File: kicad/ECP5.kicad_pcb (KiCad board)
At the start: 4 copper layers, 64.4 x 54.6 mm, 28 parts, among them J1 FLE-126-01-G-DV, SW1 PTS645SK43SMTR92 LFS

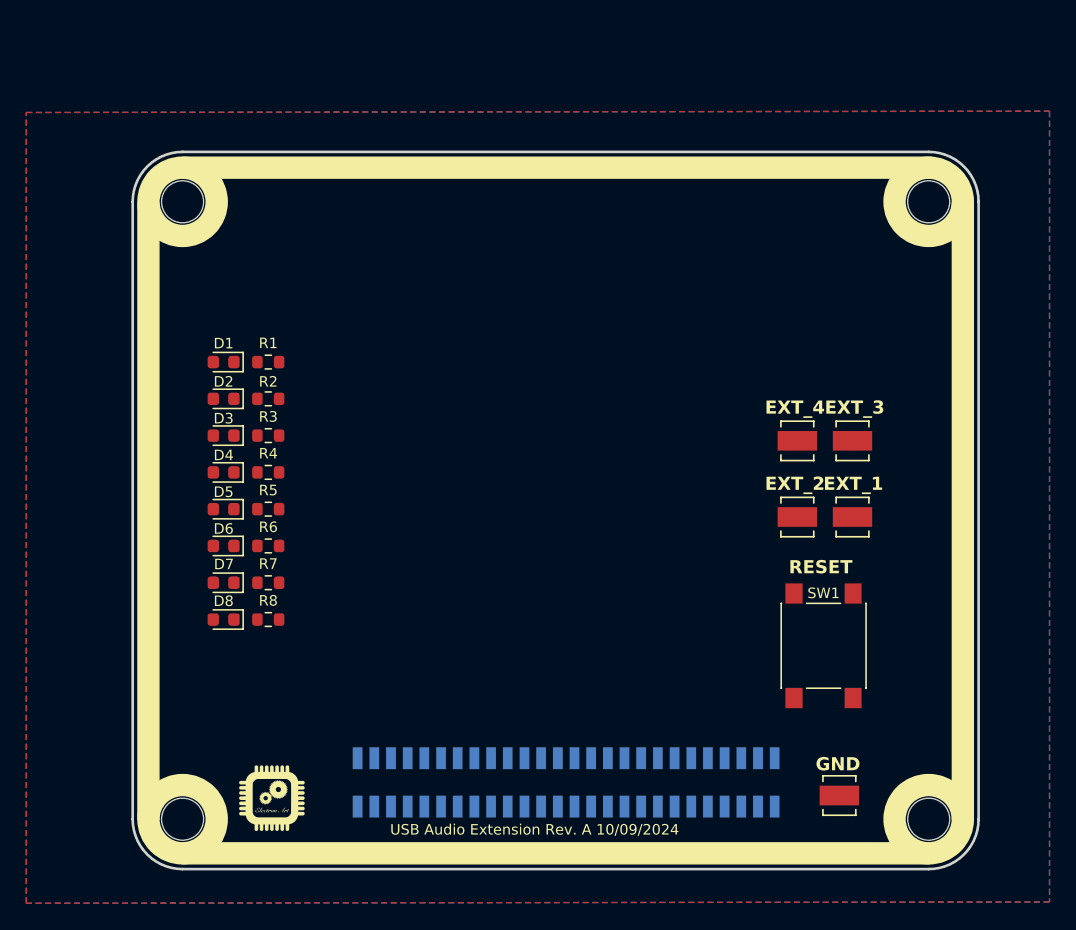
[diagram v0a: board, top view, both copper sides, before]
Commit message: First pass at arranging components
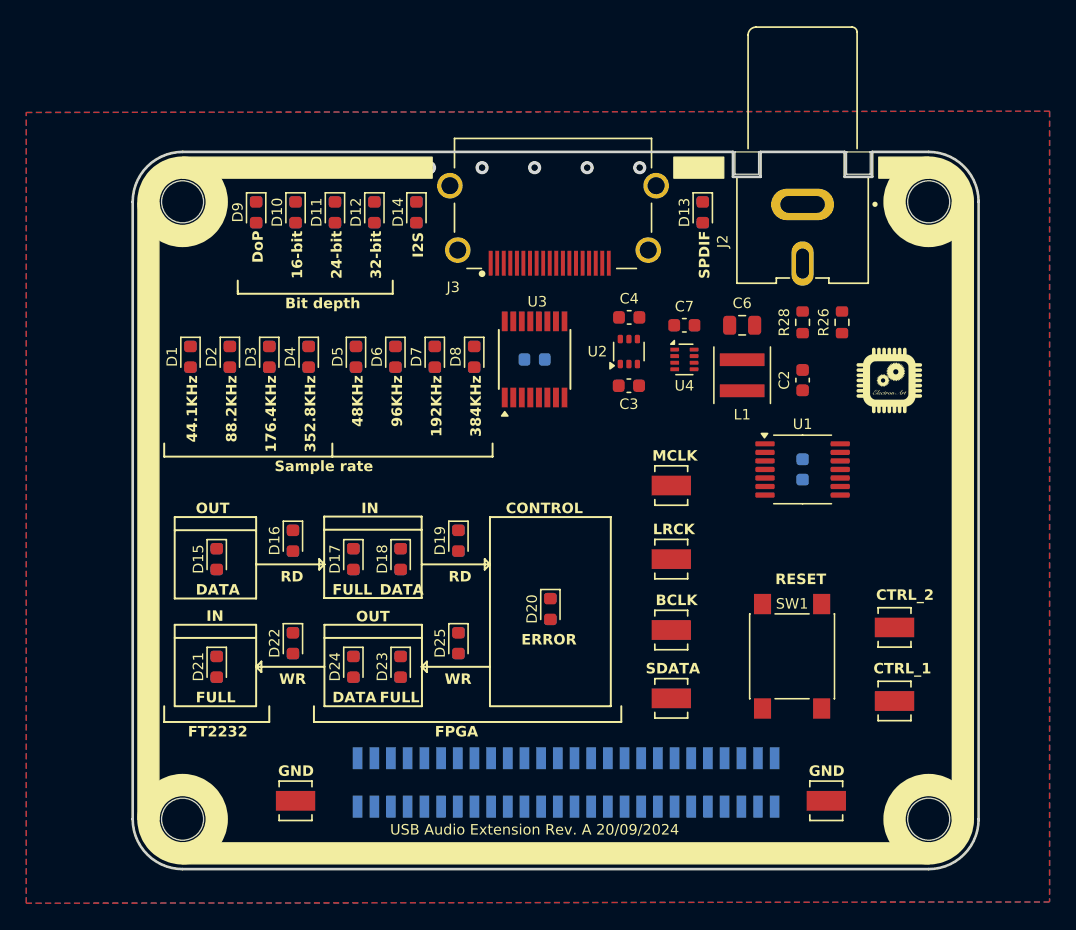
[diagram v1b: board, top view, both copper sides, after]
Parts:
- added C1: 0.1µF, Capacitor_SMD:C_0603_1608Metric, B.Cu at (168.0, 93.6)
- added C2: 0.1µF, Capacitor_SMD:C_0603_1608Metric, F.Cu at (168.0, 86.8)
- added C3: 4.7µF, Capacitor_SMD:C_0603_1608Metric, F.Cu at (154.8, 87.2)
- added C4: 18nF, Capacitor_SMD:C_0603_1608Metric, F.Cu at (154.8, 82.0)
- added C5: 0.1µF, Capacitor_SMD:C_0603_1608Metric, B.Cu at (147.6, 85.2)
- added C6: 10µF, Capacitor_SMD:C_0805_2012Metric, F.Cu at (163.4, 82.6)
- added C7: 4.7µF, Capacitor_SMD:C_0603_1608Metric, F.Cu at (159.0, 82.6)
- added D10: BLUE, LED_SMD:LED_0603_1608Metric, F.Cu at (129.4, 74.0)
- added D11: BLUE, LED_SMD:LED_0603_1608Metric, F.Cu at (132.4, 74.0)
- added D12: BLUE, LED_SMD:LED_0603_1608Metric, F.Cu at (135.4, 74.0)
- added D13: GREEN, LED_SMD:LED_0603_1608Metric, F.Cu at (160.4, 74.0)
- added D14: GREEN, LED_SMD:LED_0603_1608Metric, F.Cu at (138.6, 74.0)
- added D15: GREEN, LED_SMD:LED_0603_1608Metric, F.Cu at (123.4, 100.4)
- added D16: GREEN, LED_SMD:LED_0603_1608Metric, F.Cu at (129.2, 99.0)
- added D17: YELLOW, LED_SMD:LED_0603_1608Metric, F.Cu at (133.8, 100.4)
- added D18: GREEN, LED_SMD:LED_0603_1608Metric, F.Cu at (137.4, 100.4)
- added D19: BLUE, LED_SMD:LED_0603_1608Metric, F.Cu at (141.8, 99.0)
- added D20: RED, LED_SMD:LED_0603_1608Metric, F.Cu at (148.8, 104.2)
- added D21: YELLOW, LED_SMD:LED_0603_1608Metric, F.Cu at (123.4, 108.6)
- added D22: GREEN, LED_SMD:LED_0603_1608Metric, F.Cu at (129.2, 106.8)
- added D23: YELLOW, LED_SMD:LED_0603_1608Metric, F.Cu at (137.4, 108.6)
- added D24: GREEN, LED_SMD:LED_0603_1608Metric, F.Cu at (133.8, 108.6)
- added D25: BLUE, LED_SMD:LED_0603_1608Metric, F.Cu at (141.8, 106.8)
- added D9: BLUE, LED_SMD:LED_0603_1608Metric, F.Cu at (126.4, 74.0)
- added J2: RCJ-044, ECP5_BGA381_FT2232HQ_FIFO_EXT:CUI_RCJ-042, F.Cu at (168.0, 69.4)
- added J3: HDMI_A, ECP5_BGA381_FT2232HQ_FIFO_EXT:AMPHENOL_10029449-001RLF, F.Cu at (149.0, 76.9)
- added L1: 1µH, Inductor_SMD:L_Coilcraft_XxL4040, F.Cu at (163.4, 86.4)
- added R10: 330, Resistor_SMD:R_0603_1608Metric, B.Cu at (129.4, 74.0)
- added R11: 330, Resistor_SMD:R_0603_1608Metric, B.Cu at (132.4, 74.0)
- added R12: 330, Resistor_SMD:R_0603_1608Metric, B.Cu at (135.4, 74.0)
- added R13: 330, Resistor_SMD:R_0603_1608Metric, B.Cu at (160.4, 74.0)
- added R14: 330, Resistor_SMD:R_0603_1608Metric, B.Cu at (138.6, 74.0)
- added R15: 330, Resistor_SMD:R_0603_1608Metric, B.Cu at (123.4, 100.4)
- added R16: 330, Resistor_SMD:R_0603_1608Metric, B.Cu at (129.2, 99.0)
- added R17: 750, Resistor_SMD:R_0603_1608Metric, B.Cu at (133.8, 100.4)
- added R18: 330, Resistor_SMD:R_0603_1608Metric, B.Cu at (137.4, 100.4)
- added R20: 750, Resistor_SMD:R_0603_1608Metric, B.Cu at (148.8, 104.2)
- added R21: 750, Resistor_SMD:R_0603_1608Metric, B.Cu at (123.4, 108.6)
- added R22: 330, Resistor_SMD:R_0603_1608Metric, B.Cu at (129.2, 106.8)
- added R23: 750, Resistor_SMD:R_0603_1608Metric, B.Cu at (137.4, 108.6)
- added R24: 330, Resistor_SMD:R_0603_1608Metric, B.Cu at (133.8, 108.6)
- added R26: 150, Resistor_SMD:R_0603_1608Metric, F.Cu at (171.0, 82.4)
- added R28: 75, Resistor_SMD:R_0603_1608Metric, F.Cu at (168.0, 82.4)
- added R3: 330, Resistor_SMD:R_0603_1608Metric, B.Cu at (127.4, 85.0)
- added R4: 330, Resistor_SMD:R_0603_1608Metric, B.Cu at (130.4, 85.0)
- added R9: 330, Resistor_SMD:R_0603_1608Metric, B.Cu at (126.4, 74.0)
- added TP5: 5190TR, ECP5_BGA381_FT2232HQ_FIFO_EXT:KEYSTONE_5197TR, F.Cu at (158.0, 100.4)
- added TP6: 5190TR, ECP5_BGA381_FT2232HQ_FIFO_EXT:KEYSTONE_5197TR, F.Cu at (158.0, 94.8)
- added TP8: 5191TR, ECP5_BGA381_FT2232HQ_FIFO_EXT:KEYSTONE_5197TR, F.Cu at (129.4, 118.8)
- added U1: 74HC04, Package_SO:TSSOP-14_4.4x5mm_P0.65mm, F.Cu at (168.0, 93.6)
- added U2: TPS22948, Package_TO_SOT_SMD:SOT-363_SC-70-6, F.Cu at (154.8, 84.6)
- added U3: DSLVDS1047, ECP5_BGA381_FT2232HQ_FIFO_EXT:TSSOP-16-1EP_4.4x5mm_P0.65mm, F.Cu at (147.6, 85.2)
- added U4: TPS610333, ECP5_BGA381_FT2232HQ_FIFO_EXT:SOT-583-8, F.Cu at (159.0, 85.2)
- D1, D2: value YELLOW -> BLUE
- D3, D4: value GREEN -> BLUE
- D5, D6: value RED -> BLUE
- R1, R2, R5, R6: value 750 -> 330; moved to B.Cu
- R19: renamed from R3; moved to B.Cu
- R25: renamed from R4; moved to B.Cu
- R7, R8: moved to B.Cu
- TP1: value 5190TR -> 51907R
- TP2: value 5190TR -> 5197TR
- TP7: renamed from TP5; value 5197TR -> 5191TR
- moved G*** 56.7 mm to (174.6, 86.8)
- moved D8 27.6 mm to (143.0, 85.0), turned to -90 degrees
- moved R8 25.4 mm to (143.0, 85.0), turned to -90 degrees
- moved D7 23.5 mm to (140.0, 85.0), turned to -90 degrees
- moved R7 21.4 mm to (140.0, 85.0), turned to -90 degrees
- moved TP1 21.1 mm to (175.0, 111.2)
- moved R25 19.5 mm to (141.8, 106.8), turned to -90 degrees
- moved D6 19.5 mm to (137.0, 85.0), turned to -90 degrees
- moved R6 17.3 mm to (137.0, 85.0), turned to -90 degrees
- moved TP3 16.8 mm to (158.0, 111.0)
- moved R19 16.5 mm to (141.8, 99.0), turned to -90 degrees
- moved TP4 16.3 mm to (158.0, 105.8)
- moved D5 15.4 mm to (134.0, 85.0), turned to -90 degrees
- moved TP2 14.6 mm to (175.0, 105.6)
- moved R5 13.4 mm to (134.0, 85.0), turned to -90 degrees
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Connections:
- D1 pad 2: EXT_45 -> EXT_40
- D2 pad 2: EXT_44 -> EXT_38
- D3 pad 2: EXT_43 -> EXT_36
- D4 pad 2: EXT_42 -> EXT_34
- D5 pad 2: EXT_41 -> EXT_32
- D6 pad 2: EXT_40 -> EXT_30
- D7 pad 2: EXT_39 -> EXT_28
- D8 pad 2: EXT_38 -> EXT_26
- J1 pad 21: EXT_27 -> unconnected-(J1-Pin_21-Pad21)
- J1 pad 23: EXT_25 -> unconnected-(J1-Pin_23-Pad23)
- J1 pad 25: EXT_23 -> unconnected-(J1-Pin_25-Pad25)
- J1 pad 27: EXT_21 -> unconnected-(J1-Pin_27-Pad27)
- J1 pad 29: EXT_19 -> unconnected-(J1-Pin_29-Pad29)
- J1 pad 31: EXT_17 -> unconnected-(J1-Pin_31-Pad31)
- J1 pad 33: EXT_15 -> unconnected-(J1-Pin_33-Pad33)
- J1 pad 35: EXT_13 -> unconnected-(J1-Pin_35-Pad35)
- J1 pad 37: EXT_11 -> unconnected-(J1-Pin_37-Pad37)
- J1 pad 39: EXT_9 -> unconnected-(J1-Pin_39-Pad39)
- J1 pad 41: EXT_7 -> unconnected-(J1-Pin_41-Pad41)
- J1 pad 43: EXT_5 -> unconnected-(J1-Pin_43-Pad43)
- J1 pad 45: EXT_3 -> unconnected-(J1-Pin_45-Pad45)
- R19 pad 1: Net-(D3-K) -> Net-(D19-K)
- R25 pad 1: Net-(D4-K) -> Net-(D25-K)
- TP1 pad 1: EXT_4 -> EXT_1
- TP2 pad 1: EXT_3 -> EXT_2
- TP3 pad 1: EXT_2 -> EXT_6
- TP4 pad 1: EXT_1 -> EXT_8
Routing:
- net GND: vias 57 -> 55
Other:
- outline, holes or cut-outs redrawn
- board text added: "16-bit"
- board text added: "176.4KHz"
- board text added: "192KHz"
- board text added: "24-bit"
- board text added: "32-bit"
- board text added: "352.8KHz"
- board text added: "384KHz"
- board text added: "44.1KHz"
- board text added: "48KHz"
- board text added: "88.2KHz"
- board text added: "96KHz"
- board text added: "BCLK"
- board text added: "Bit depth"
- board text added: "CONTROL"
- board text added: "CTRL_1"
- board text added: "CTRL_2"
- board text added: "DATA"
- board text added: "DoP"
- board text added: "ERROR"
- board text added: "FPGA"
- board text added: "FT2232"
- board text added: "FULL"
- board text added: "I2S"
- board text added: "IN"
- board text added: "LRCK"
- board text added: "MCLK"
- board text added: "OUT"
- board text added: "RD"
- board text added: "SDATA"
- board text added: "SPDIF"
- board text added: "Sample rate"
- board text added: "USB Audio Extension Rev. A 20/09/2024"
- board text added: "WR"
- board text removed: "EXT_1"
- board text removed: "EXT_2"
- board text removed: "EXT_3"
- board text removed: "EXT_4"
- board text removed: "USB Audio Extension Rev. A 10/09/2024"

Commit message: Updated the BOM
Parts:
- J3: value HDMI_A -> HDMI A
- TP1: value 51907R -> 5197TR

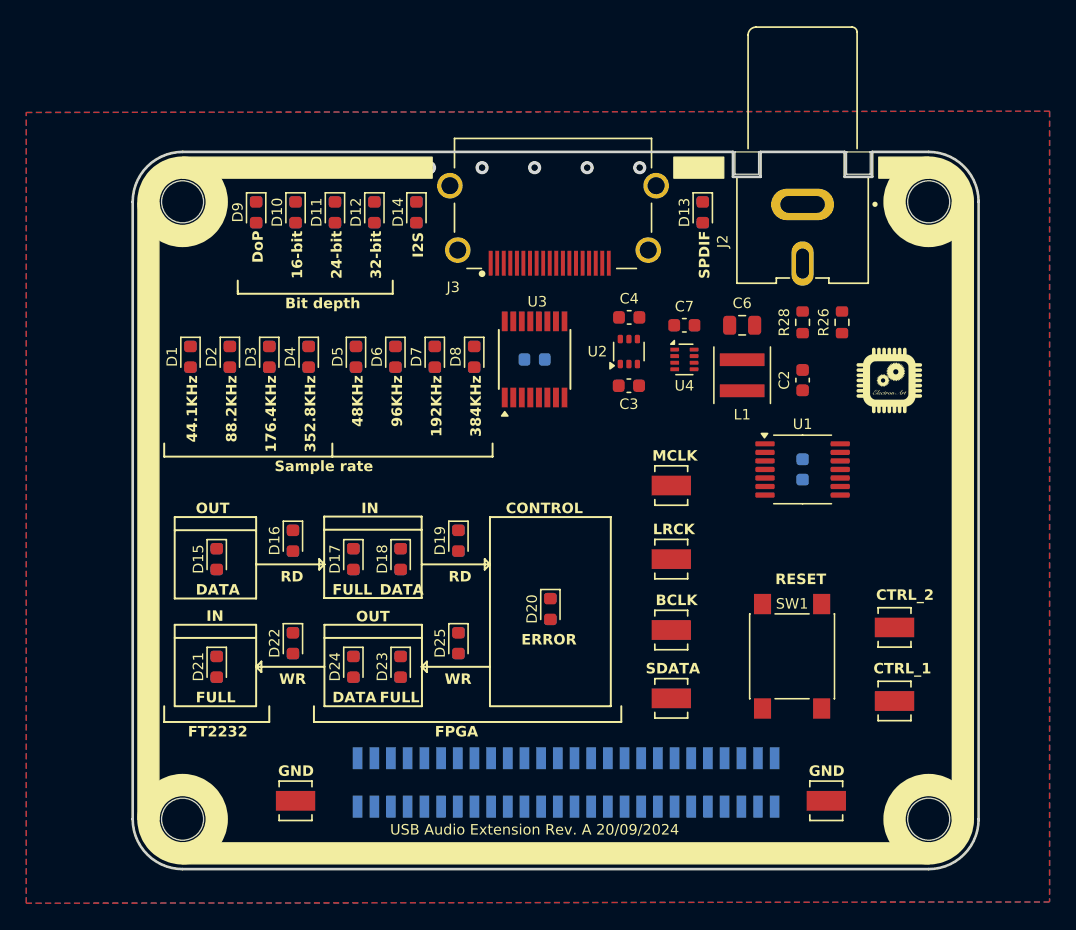
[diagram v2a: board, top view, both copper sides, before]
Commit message: Removed unused symbols and footprints
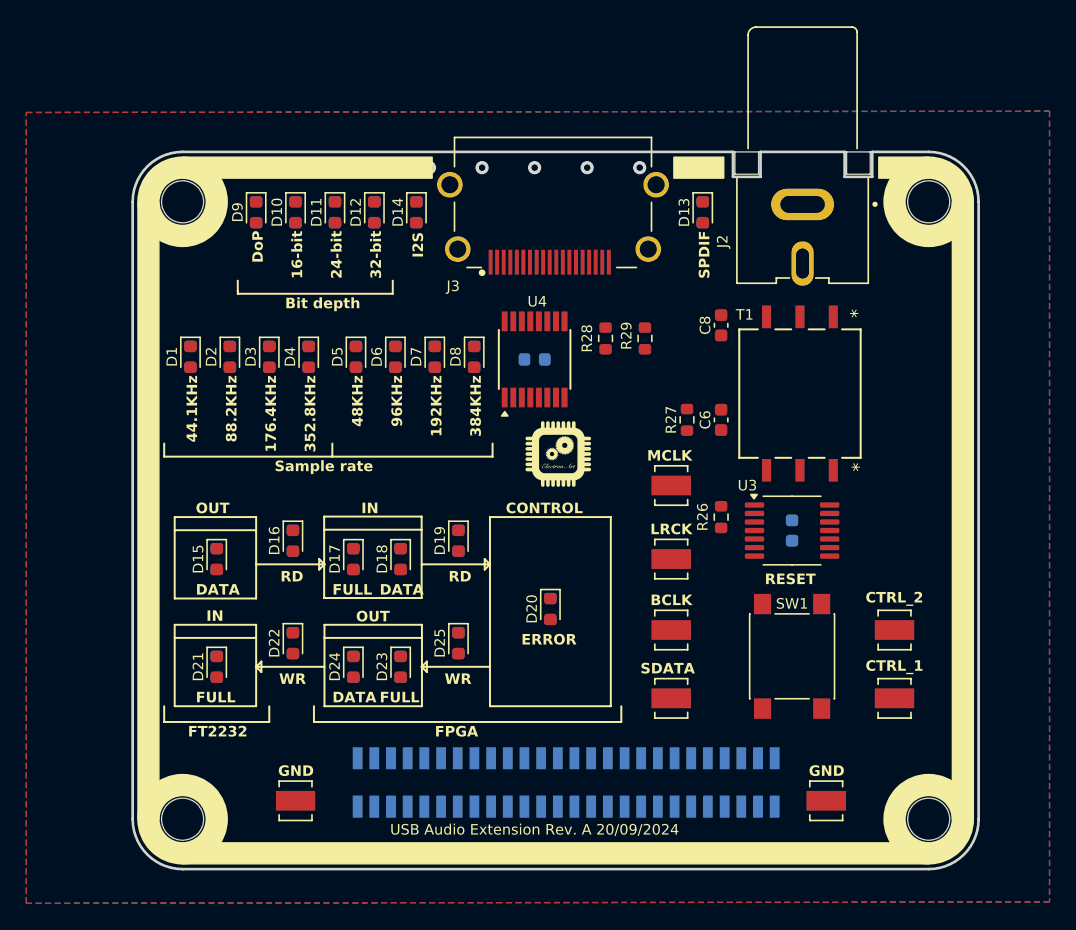
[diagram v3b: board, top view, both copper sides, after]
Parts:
- removed C3, C7: 4.7µF, Capacitor_SMD:C_0603_1608Metric
- removed the C4 at (154.8, 82.0)
- removed the C6 at (163.4, 82.6)
- removed L1: 1µH, Inductor_SMD:L_Coilcraft_XxL4040
- removed U2: TPS22948, Package_TO_SOT_SMD:SOT-363_SC-70-6
- removed the U4 at (159.0, 85.2)
- added C8: 18nF, Capacitor_SMD:C_0603_1608Metric, F.Cu at (161.8, 82.6)
- added R28: 100, Resistor_SMD:R_0603_1608Metric, F.Cu at (153.0, 83.6)
- added R29: 100, Resistor_SMD:R_0603_1608Metric, F.Cu at (156.0, 83.6)
- added T1: DA101JC, ECP5_BGA381_FT2232HQ_FIFO_EXT:DA101J_MUR, F.Cu at (167.8, 87.8)
- moved G*** 25.8 mm to (149.4, 92.4)
- moved R26 17.4 mm to (161.8, 97.2)
- moved R27 11.5 mm to (159.2, 89.8)
- moved C6 6.90 mm to (161.8, 89.8), turned to 90 degrees
- moved C5 4.72 mm to (167.2, 98.2)
- moved U3 4.72 mm to (167.2, 98.2)
- moved TP1 0.20 mm to (175.0, 111.0)
- moved TP2 0.20 mm to (175.0, 105.8)
- moved J3 0.08 mm to (149.0, 76.8)
- renumbered C5 to C4, C1 to C5, C2 to C6, R28 to R27, U1 to U3, U3 to U4
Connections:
- C6 pad 1: Net-(J2-In) -> Net-(T1-SB)
- J1 pad 37: unconnected-(J1-Pin_37-Pad37) -> EXT_11
- J1 pad 39: unconnected-(J1-Pin_39-Pad39) -> EXT_9
- J2 pad 1: GND -> Net-(J2-Ext)
- J3 pad 15: unconnected-(J3-SCL-Pad15) -> Net-(J3-SCL)
- J3 pad 16: unconnected-(J3-SDA-Pad16) -> Net-(J3-SDA)
- J3 pad 18: Net-(J3-+5V) -> unconnected-(J3-+5V-Pad18)

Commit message: First routing
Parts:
- added TP9: 5194TR, ECP5_BGA381_FT2232HQ_FIFO_EXT:KEYSTONE_5197TR, F.Cu at (158.0, 86.0)
- moved R29 1.28 mm to (155.2, 82.6)
- moved R28 1.17 mm to (152.4, 82.6)
- moved C5 0.80 mm to (168.0, 98.2)
- moved SW1 0.80 mm to (168.0, 107.8)
- moved U3 0.80 mm to (168.0, 98.2)
- moved TP8 0.50 mm to (129.9, 118.8)
- moved C8 0.20 mm to (161.8, 82.8)
- moved T1 0.20 mm to (168.0, 87.8)
- turned C6 to -90 degrees
- turned R27 to 90 degrees
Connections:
- TP3 pad 1: EXT_6 -> EXT_12
- TP4 pad 1: EXT_8 -> EXT_10
- TP5 pad 1: EXT_10 -> EXT_8
- TP6 pad 1: EXT_12 -> EXT_6
- U4 pad 2: EXT_6 -> EXT_12
- U4 pad 3: EXT_8 -> EXT_10
- U4 pad 6: EXT_10 -> EXT_8
- U4 pad 7: EXT_12 -> EXT_6
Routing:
- net GND: track 0.00 -> 76.6 mm, vias 55 -> 95
- net EXT_24: track 0.00 -> 52.7 mm, vias 0 -> 1
- net EXT_22: track 0.00 -> 50.4 mm, vias 0 -> 1
- net EXT_20: track 0.00 -> 49.2 mm, vias 0 -> 1
- net EXT_18: track 0.00 -> 48.1 mm, vias 0 -> 1
- net EXT_16: track 0.00 -> 46.8 mm, vias 0 -> 1
- net EXT_14: track 0.00 -> 43.6 mm, vias 0 -> 1
- net EXT_11: track 0.00 -> 41.4 mm, vias 0 -> 3
- net EXT_9: track 0.00 -> 40.7 mm, vias 0 -> 3
- net EXT_40: track 0.00 -> 37.3 mm, vias 0 -> 1
- net EXT_38: track 0.00 -> 35.9 mm, vias 0 -> 1
- net EXT_36: track 0.00 -> 35.2 mm, vias 0 -> 1
- net EXT_12: track 0.00 -> 34.7 mm, vias 0 -> 1
- net EXT_34: track 0.00 -> 34.5 mm, vias 0 -> 1
- net EXT_6: track 0.00 -> 34.2 mm, vias 0 -> 1
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- added copper zone on In2.Cu, net +3V3
- removed copper zone on In2.Cu, net GND

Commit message: Updated PCB
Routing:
- net GND: vias 95 -> 96
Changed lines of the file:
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@@
+	)
+	(via
+		(at 171.9 122.8)
+		(size 1)
+		(drill 0.5)
+		(layers "F.Cu" "B.Cu")
+		(free yes)
+		(net 2)
 	)
 	(via
